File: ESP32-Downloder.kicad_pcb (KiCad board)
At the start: 2 copper layers, 20 x 35 mm, 21 parts, among them J1 USB_C_Receptacle_USB2.0_16P, J2 ESP32_DOWNLOAD_CON, Q1 BSS138, Q2 BSS138, SW1 RESET, SW2 FLASH, U1 CH340K, U2 AMS1117-3.3

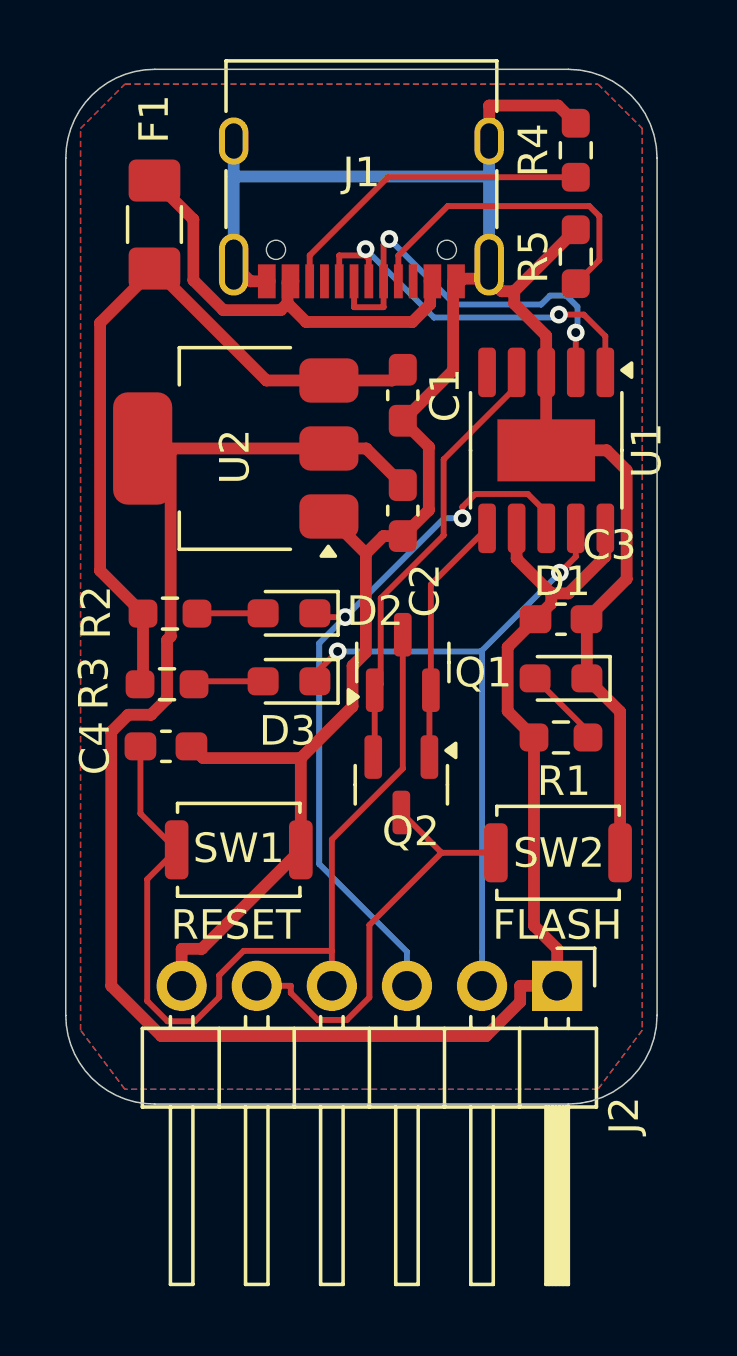
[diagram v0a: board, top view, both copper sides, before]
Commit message: README追加、ガーバーデータ出力
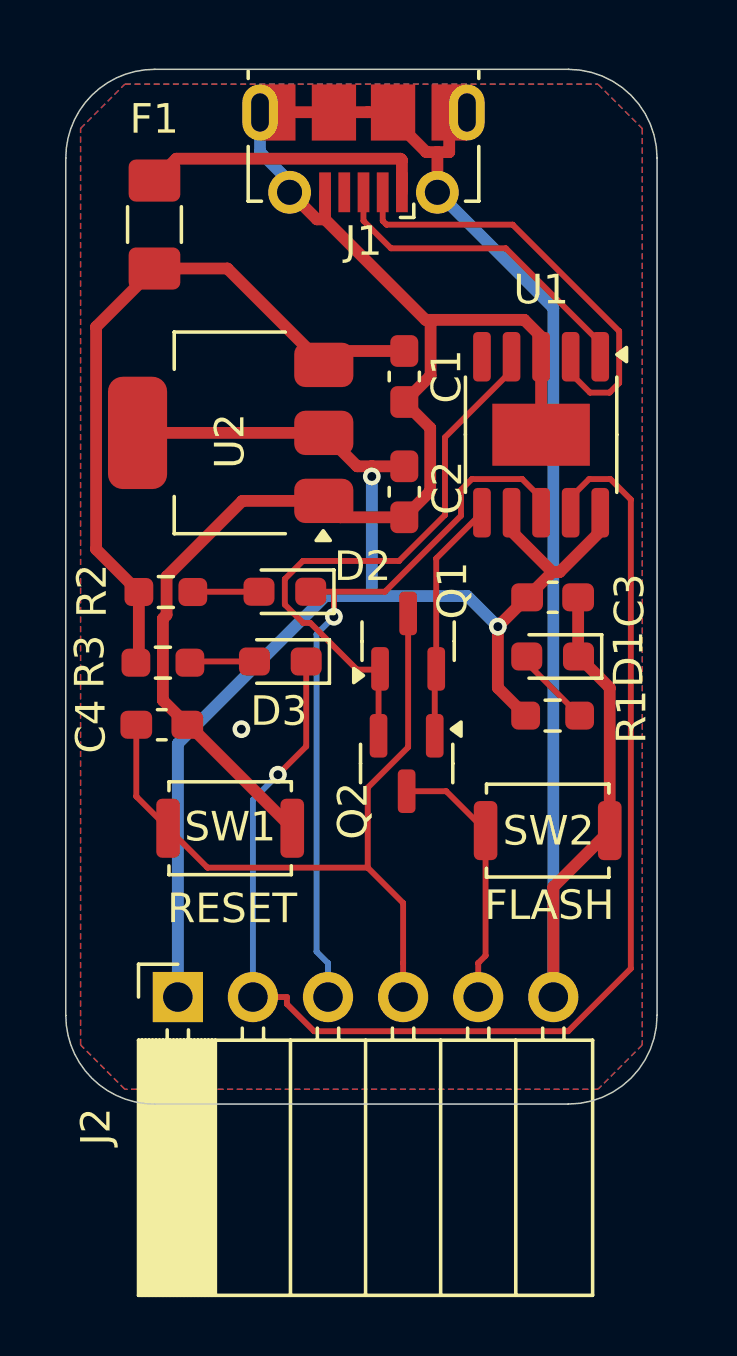
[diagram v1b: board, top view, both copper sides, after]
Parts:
- removed R4, R5: 5.1k, Resistor_SMD:R_0603_1608Metric_Pad0.98x0.95mm_HandSolder
- J1: value USB_C_Receptacle_USB2.0_16P -> USB_B_Micro; footprint Connector_USB:USB_C_Receptacle_XKB_U262-16XN-4BVC11 -> Connector_USB:USB_Micro-B_Molex-105017-0001
- J2: footprint Connector_PinHeader_2.54mm:PinHeader_1x06_P2.54mm_Horizontal -> Connector_PinSocket_2.54mm:PinSocket_1x06_P2.54mm_Horizontal
- moved J2 12.8 mm to (113.8, 71.4), turned to 90 degrees
- moved SW2 0.83 mm to (126.3, 65.8)
- moved J1 0.81 mm to (120.1, 42.7)
- moved C3 0.79 mm to (126.5, 57.9)
- moved D1 0.79 mm to (126.5, 59.9)
- moved R1 0.79 mm to (126.5, 61.9)
- moved SW1 0.79 mm to (115.6, 65.7)
- moved C4 0.74 mm to (113.2, 62.2)
- moved D2 0.74 mm to (117.4, 57.7)
- moved R2 0.74 mm to (113.4, 57.7)
- moved R3 0.74 mm to (113.3, 60.1)
- moved Q2 0.74 mm to (121.5, 63.5)
- moved Q1 0.74 mm to (121.6, 59.3)
- moved D3 0.73 mm to (117.3, 60.0)
- moved C1 0.64 mm to (121.5, 50.4)
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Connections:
- F1 pad 1: Net-(F1-Pad1) -> Net-(J1-VBUS)
- U1 pad 1: Net-(U1-UD+) -> Net-(J1-D+)
- U1 pad 2: Net-(U1-UD-) -> Net-(J1-D-)
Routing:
- net /RXD: track 23.0 -> 45.3 mm, vias 2 -> 1
- net +3.3V: track 66.1 -> 47.2 mm, vias 0 -> 2
- net Net-(F1-Pad1): track 15.1 -> 0.00 mm
- net Net-(J1-D-): track 0.00 -> 14.9 mm
- net Net-(U1-UD-): track 14.1 -> 0.00 mm, vias 2 -> 0
- net Net-(U1-UD+): track 13.5 -> 0.00 mm, vias 2 -> 0
- net GND: track 86.2 -> 99.7 mm, vias 0 -> 1
- net Net-(J1-D+): track 0.00 -> 11.2 mm
- net Net-(J1-CC1): track 11.1 -> 0.00 mm
- net Net-(J1-CC2): track 11.0 -> 0.00 mm
- net Net-(J1-VBUS): track 0.00 -> 9.77 mm
- net /GPIO0: track 14.4 -> 8.96 mm
- net /EN: track 30.4 -> 25.3 mm
- net Net-(Q1-G): track 15.0 -> 19.8 mm
- net /VBUS: track 25.6 -> 24.8 mm
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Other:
- board text added: "3.3V"
- board text added: "EN"
- board text added: "ESP32 Downloader REV1 KUNI-NET 2025"
- board text added: "G0"
- board text added: "GND"
- board text added: "RxD"
- board text added: "TxD"
